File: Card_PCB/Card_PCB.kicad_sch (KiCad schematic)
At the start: 19 parts

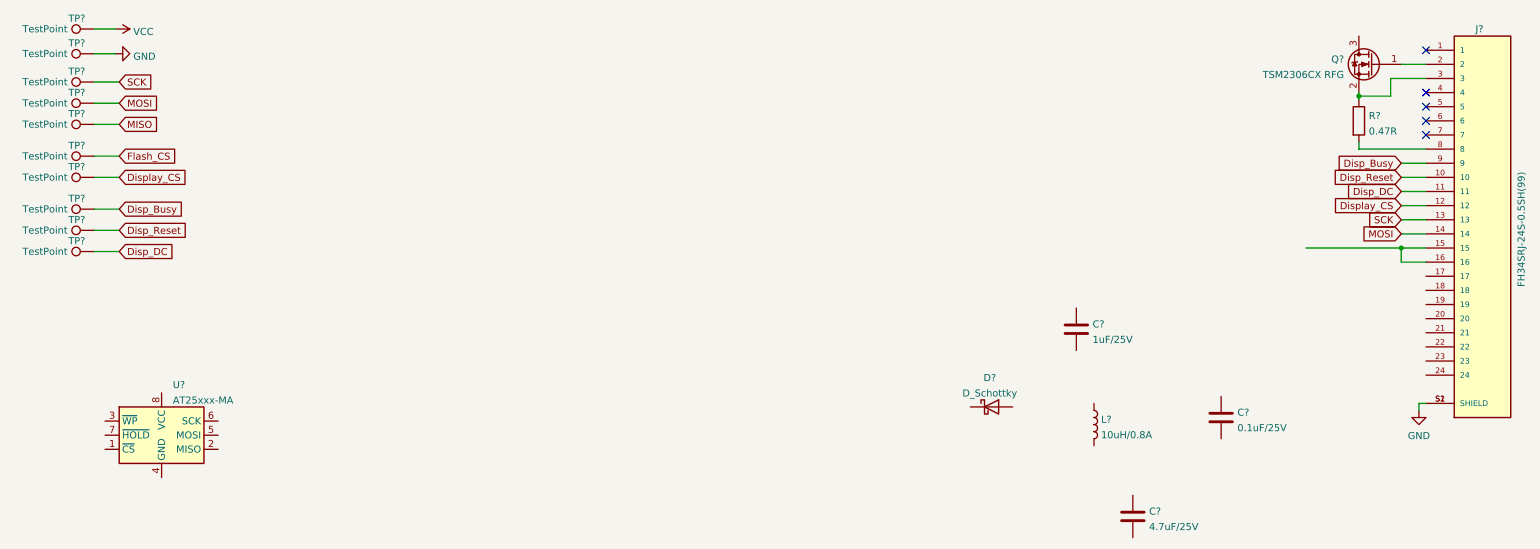
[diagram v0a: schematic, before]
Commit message: updated schematics and PCB
Fixed issues between datasheet circuit and my PCB
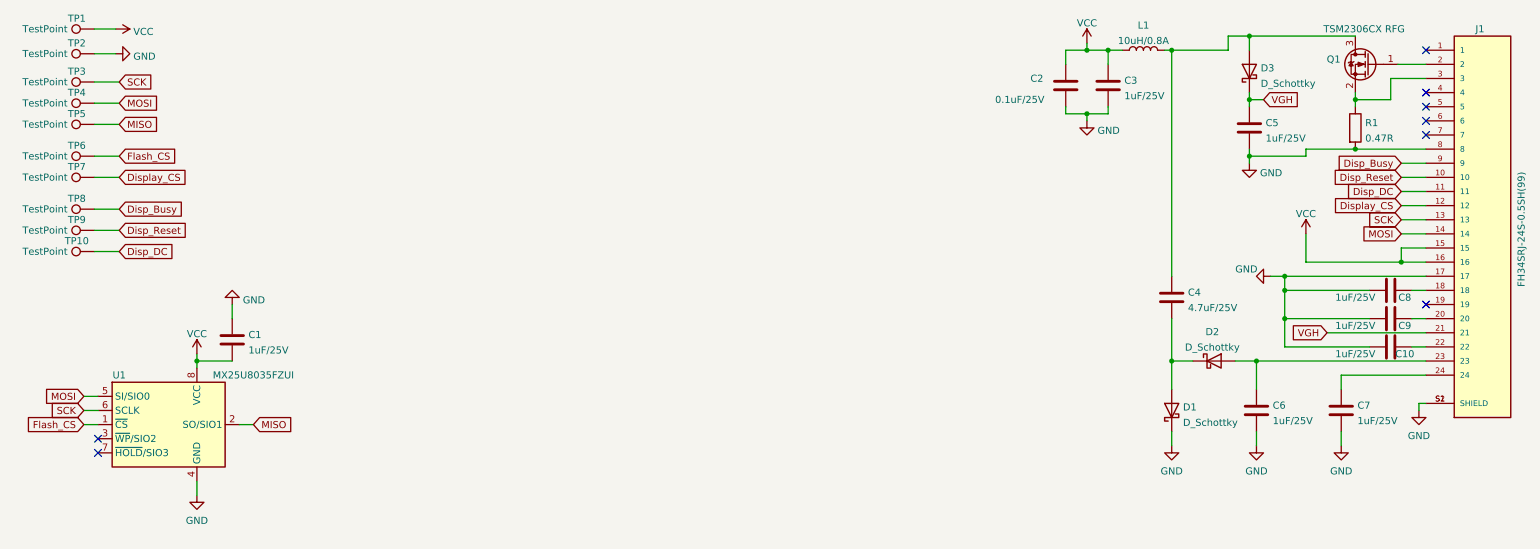
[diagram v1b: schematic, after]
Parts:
- removed C?: 0.1uF/25V, symbol Device:C
- removed C?: 1uF/25V, symbol Device:C
- removed C?: 4.7uF/25V, symbol Device:C
- removed D?: D_Schottky, symbol Device:D_Schottky
- removed U?: AT25xxx-MA, Package_DFN_QFN:DFN-8-1EP_3x2mm_P0.5mm_EP1.75x1.45mm, symbol Memory_EEPROM:AT25xxx-MA
- added C1, C10, C3, C5, C6, C7, C8, C9: 1uF/25V, Capacitor_SMD:C_0603_1608Metric, symbol Device:C
- added C2: 0.1uF/25V, Capacitor_SMD:C_0603_1608Metric, symbol Device:C
- added C4: 4.7uF/25V, Capacitor_SMD:C_0603_1608Metric, symbol Device:C
- added D1, D2, D3: D_Schottky, Diode_SMD:D_SOD-123F, symbol Device:D_Schottky
- added U1: MX25U8035FZUI, Package_SON:SON-8-1EP_3x2mm_P0.5mm_EP1.4x1.6mm, symbol Memory_Flash:MX25R3235FM1xx1
- J1: renamed from J?; footprint HRS_FH34SRJ-24S-0.5SH(99) -> Created_Parts:FH34SRJ_24S
- L1: renamed from L?; footprint (none) -> Inductor_SMD:L_Taiyo-Yuden_MD-4040
- Q1: renamed from Q?; footprint (none) -> Package_TO_SOT_SMD:SOT-23
- R1: renamed from R?; footprint (none) -> Resistor_SMD:R_0603_1608Metric
- TP1, TP10, TP2, TP3, TP4, TP5, TP6, TP7, TP8, TP9: renamed from TP?; footprint (none) -> TestPoint:TestPoint_Pad_2.0x2.0mm
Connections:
- net Flash_CS: now also U1.1 (~{CS})
- net GND: now also J1.17, J1.8, R1.2, C1.1, C10.1, C2.1, C3.2, C5.2, C6.2, C7.2, C8.1, C9.1, D1.1 (K), U1.4 (GND)
- net MISO: now also U1.2 (SO/SIO1)
- net MOSI: now also U1.5 (SI/SIO0)
- net SCK: now also U1.6 (SCLK)
- net VCC: now also J1.15, J1.16, L1.1, C1.2, C2.2, C3.1, U1.8 (VCC)
- net at Q1.3 (D): now also L1.2, C4.1, D3.2 (A)
- net at J1.18: now also C8.2
- net at J1.20: now also C9.2
- net VGH: now reaches J1.21
- net VGH: now also C5.1, D3.1 (K)
- net at J1.22: now also C10.2
- net at J1.23: now also C6.1, D2.2 (A)
- net at J1.24: now also C7.1
- new net: C4.2, D1.2 (A), D2.1 (K)
- no-connect marks 5 -> 8
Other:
- moved on the sheet: L1, Q1, R1
